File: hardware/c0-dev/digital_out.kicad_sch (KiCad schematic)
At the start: 27 parts, among them Q10 BSS138P, Q3 BSS138P, Q4 BSS138P, Q5 BSS138P, Q6 BSS138P, Q7 BSS138P, Q8 BSS138P, Q9 BSS138P, U34 B0505S-1WR3, U35 ISO1540, U36 TCA9555PWR, U48 TLP175A

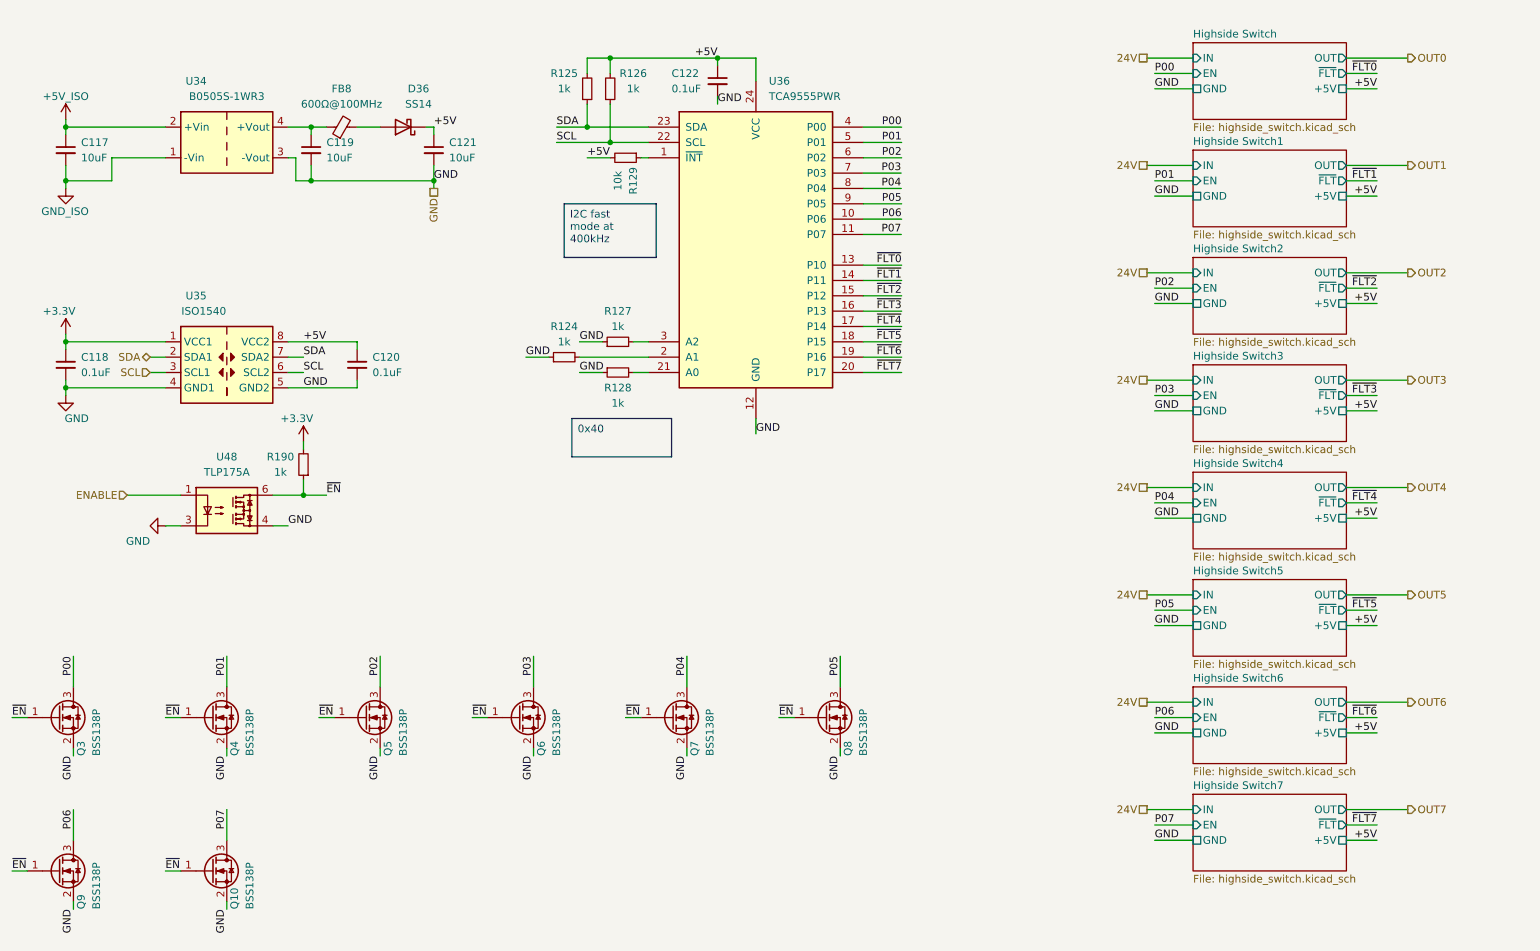
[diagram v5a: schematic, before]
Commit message: added 4-pin connector
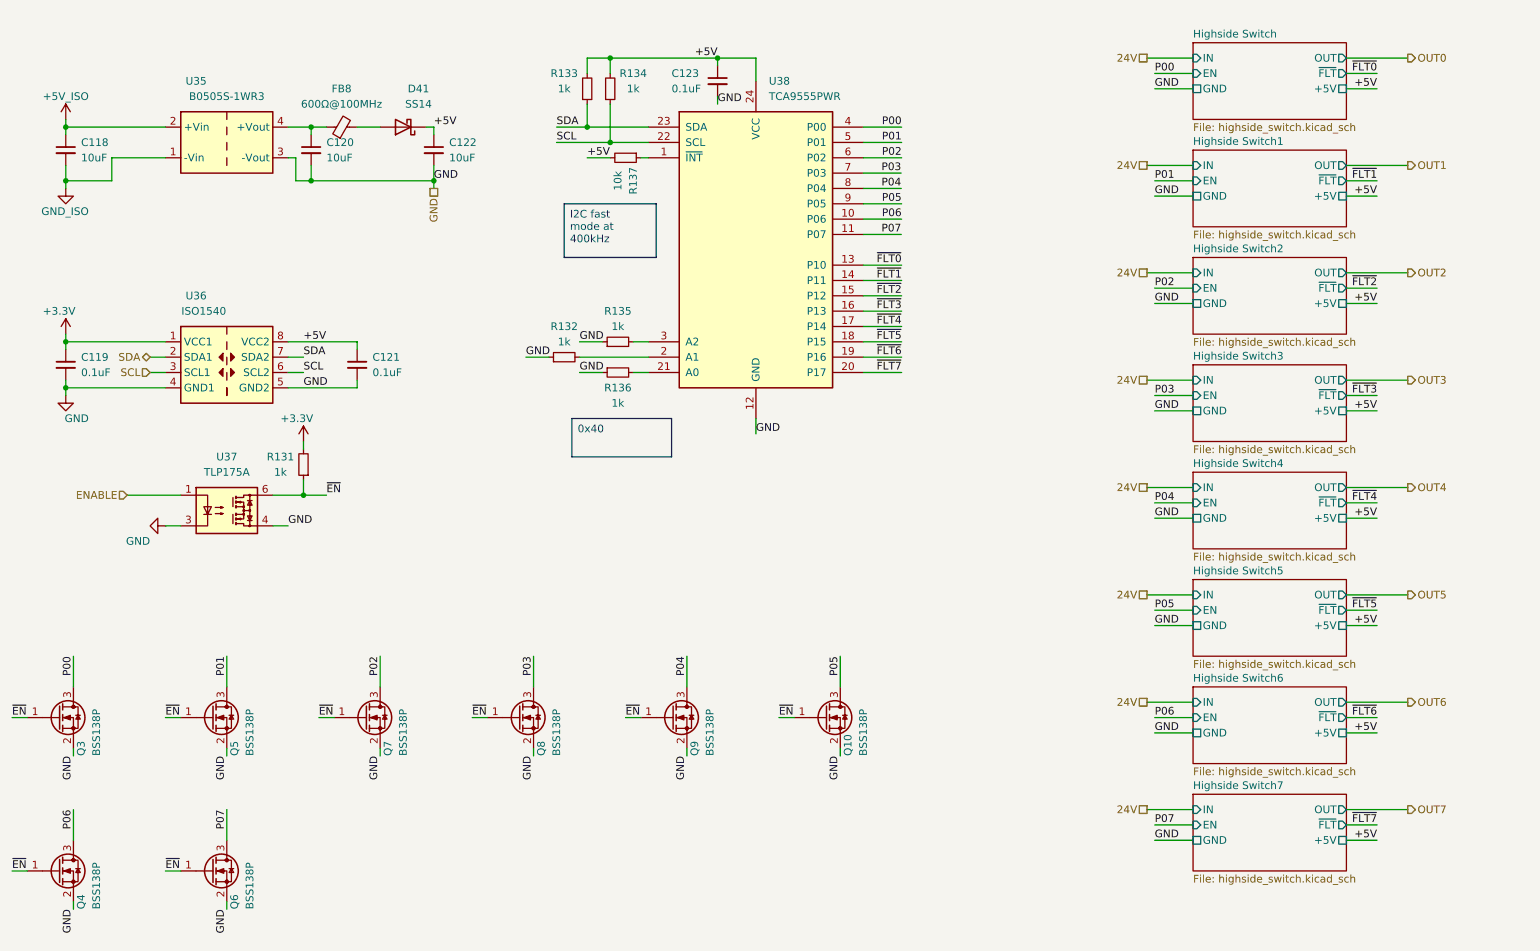
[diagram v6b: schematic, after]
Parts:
- renumbered C117 to C118, C118 to C119, C119 to C120, C120 to C121, C121 to C122, C122 to C123, D36 to D41, Q8 to Q10, Q9 to Q4, Q4 to Q5, Q10 to Q6, Q5 to Q7, Q6 to Q8, Q7 to Q9, R190 to R131, R124 to R132, R125 to R133, R126 to R134, R127 to R135, R128 to R136, R129 to R137, U34 to U35, U35 to U36, U48 to U37, U36 to U38

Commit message: annotation + new digital out
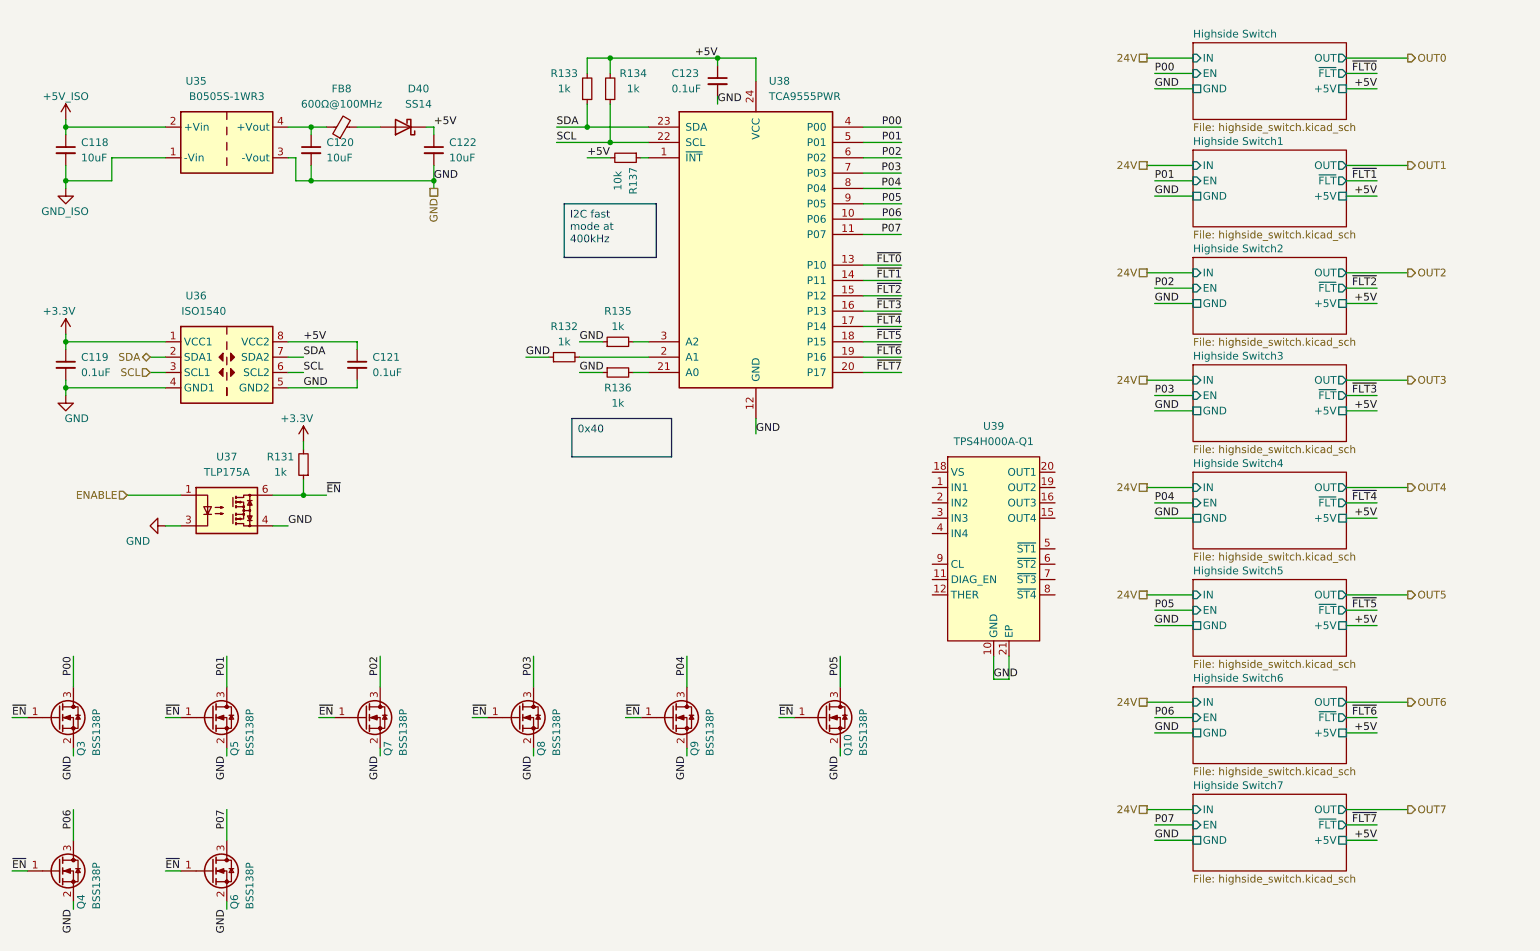
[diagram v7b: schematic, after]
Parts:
- added U39: TPS4H000A-Q1, Package_SO:ETSSOP-20-1EP_4.4x6.5mm_P0.65mm_EP3x4.2mm, symbol conduit:TPS4H000A-Q1
- renumbered D41 to D40
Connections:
- net GND: now also U39.10 (GND), U39.21 (EP)
- new net: U39.13 (NC), U39.14 (NC)
- new net VS: U39.17 (VS), U39.18 (VS)
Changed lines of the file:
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@@
 	(wire
 		(pts
+			(xy 193.04 127) (xy 193.04 123.19)
+		)
+		(stroke
+			(width 0)
+			(type default)
+		)
+	)
+	(wire
+		(pts
+			(xy 190.5 123.19) (xy 190.5 127)
+		)
+		(stroke
+			(width 0)
+			(type default)
+		)
+	)
+	(wire
+		(pts
 			(xy 97.79 44.45) (xy 97.79 45.72)
 		)
@@
 	(wire
 		(pts
+			(xy 190.5 127) (xy 193.04 127)
+		)
+		(stroke
+			(width 0)
+			(type default)
+		)
+	)
+	(wire
+		(pts
 			(xy 248.92 95.25) (xy 259.08 95.25)
 		)
@@
 		)
 	)
+	(label "GND"
+		(at 190.5 127 0)
+		(effects
+			(font
+				(size 1.27 1.27)
+			)
+			(justify left bottom)
+		)
+	)
 	(label "+5V"
 		(at 97.79 35.56 0)
@@
 	)
 	(symbol
+		(lib_id "conduit:TPS4H000A-Q1")
+		(at 190.5 104.14 0)
+		(unit 1)
+		(body_style 1)
+		(exclude_from_sim no)
+		(in_bom yes)
+		(on_board yes)
+		(in_pos_files yes)
+		(dnp no)
+		(fields_autoplaced yes)
+		(property "Reference" "U39"
+			(at 190.5 85.09 0)
+			(show_name no)
+			(do_not_autoplace no)
+			(effects
+				(font
+					(size 1.27 1.27)
+				)
+			)
+		)
+		(property "Value" "TPS4H000A-Q1"
+			(at 190.5 87.63 0)
+			(show_name no)
+			(do_not_autoplace no)
+			(effects
+				(font
+					(size 1.27 1.27)
+				)
+			)
+		)
+		(property "Footprint" "Package_SO:ETSSOP-20-1EP_4.4x6.5mm_P0.65mm_EP3x4.2mm"
+			(at 190.754 79.756 0)
+			(hide yes)
+			(show_name no)
+			(do_not_autoplace no)
+			(effects
+				(font
+					(size 1.27 1.27)
+				)
+			)
+		)
+		(property "Datasheet" "https://www.ti.com/lit/ds/symlink/tps4h000-q1.pdf"
+			(at 189.23 77.216 0)
+			(hide yes)
+			(show_name no)
+			(do_not_autoplace no)
+			(effects
+				(font
+					(size 1.27 1.27)
+				)
+			)
+		)
+		(property "Description" "40-V, 1-Ω, 4-ch automotive smart high-side switch with adjustable current limit"
+			(at 190.246 82.296 0)
+			(hide yes)
+			(show_name no)
+			(do_not_autoplace no)
+			(effects
+				(font
+					(size 1.27 1.27)
+				)
+			)
+		)
+		(property "JLCPCB Part" "C2680315"
+			(at 189.23 77.47 0)
+			(hide yes)
+			(show_name no)
+			(do_not_autoplace no)
+			(effects
+				(font
+					(size 1.27 1.27)
+				)
+			)
+		)
+		(pin "14"
+		)
+		(pin "13"
+		)
+		(pin "6"
+		)
+		(pin "12"
+		)
+		(pin "4"
+		)
+		(pin "3"
+		)
+		(pin "9"
+		)
+		(pin "10"
+		)
+		(pin "1"
+		)
+		(pin "2"
+		)
+		(pin "7"
+		)
+		(pin "8"
+		)
+		(pin "11"
+		)
+		(pin "5"
+		)
+		(pin "15"
+		)
+		(pin "16"
+		)
+		(pin "17"
+		)
+		(pin "18"
+		)
+		(pin "19"
+		)
+		(pin "20"
+		)
+		(pin "21"
+		)
+		(instances
+			(project "c0-dev"
+				(path "/b8347a0e-ad04-4414-969d-3c64a611d74e/680032e3-5da4-48ad-9c49-e468cbbeffb9"
+					(reference "U39")
+					(unit 1)
+				)
+			)
+		)
+	)
+	(symbol
 		(lib_id "Device:C_Small")
 		(at 144.78 27.94 0)
@@
 		(in_pos_files yes)
 		(dnp no)
-		(property "Reference" "D41"
+		(property "Reference" "D40"
 			(at 95.25 29.21 0)
 			(show_name no)
@@
 			(project "c0-dev"
 				(path "/b8347a0e-ad04-4414-969d-3c64a611d74e/680032e3-5da4-48ad-9c49-e468cbbeffb9"
-					(reference "D41")
+					(reference "D40")
 					(unit 1)
 				)

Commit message: updated digital out
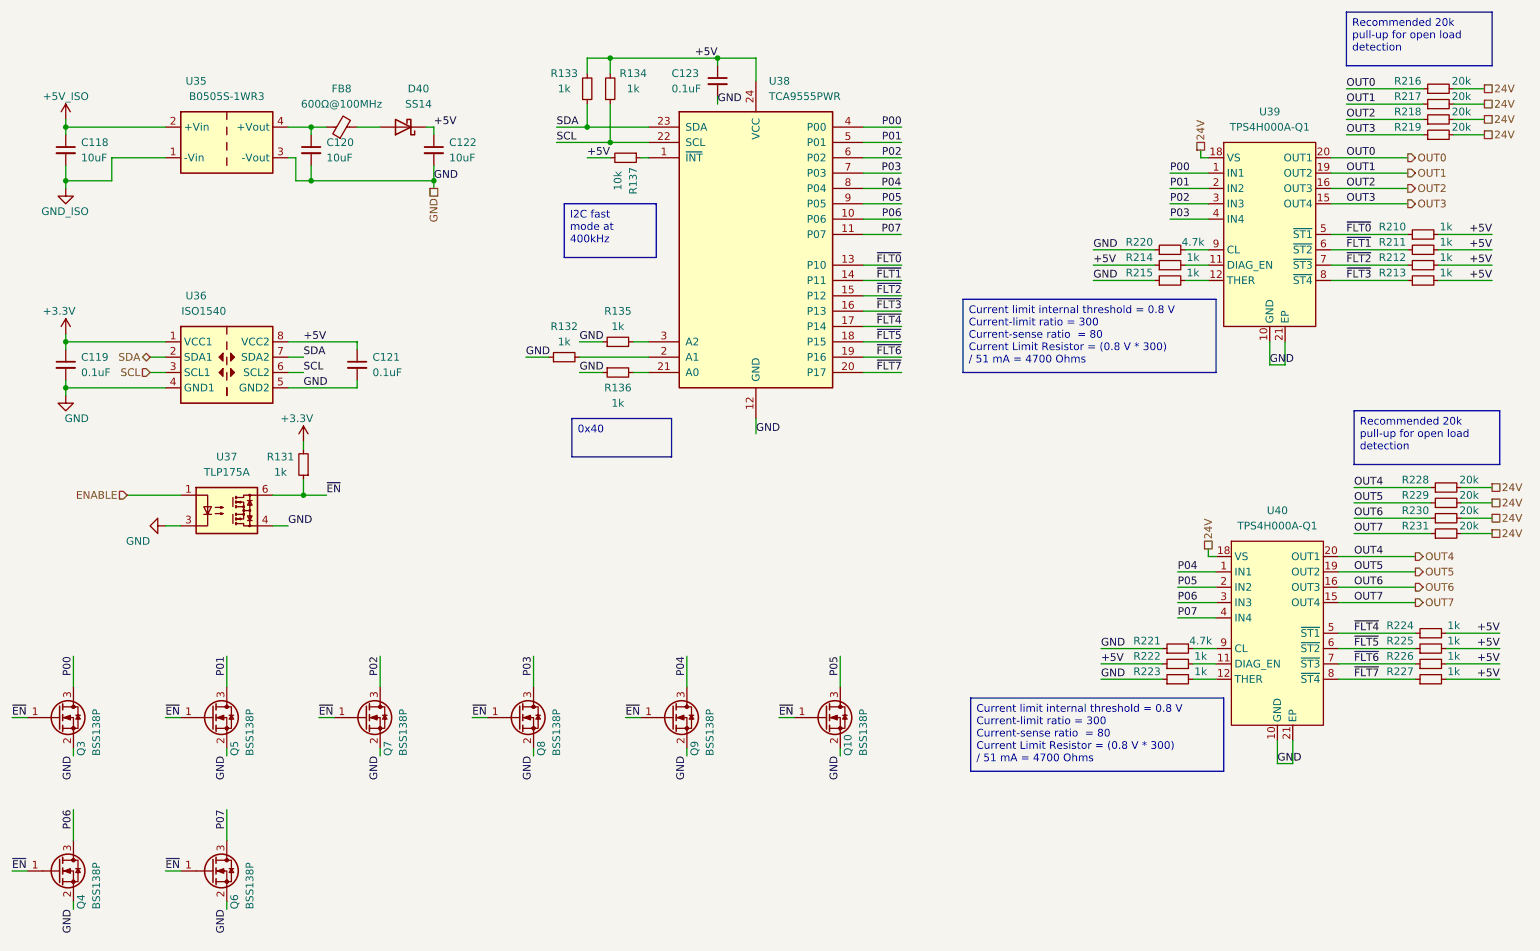
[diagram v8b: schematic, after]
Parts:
- added R210, R211, R212, R213, R214, R215, R222, R223, R224, R225, R226, R227: 1k, Resistor_SMD:R_0402_1005Metric, symbol Device:R_Small
- added R216, R217, R218, R219, R228, R229, R230, R231: 20k, Resistor_SMD:R_0402_1005Metric, symbol Device:R_Small
- added R220, R221: 4.7k, Resistor_SMD:R_0402_1005Metric, symbol Device:R_Small
- added U40: TPS4H000A-Q1, Package_SO:ETSSOP-20-1EP_4.4x6.5mm_P0.65mm_EP3x4.2mm, symbol conduit:TPS4H000A-Q1
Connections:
- net +5V: now also R210.2, R211.2, R212.2, R213.2, R214.1, R222.1, R224.2, R225.2, R226.2, R227.2
- net GND: now also R215.1, R220.1, R221.1, R223.1, U40.10 (GND), U40.21 (EP)
- net OUT0: now also U39.20 (OUT1), R216.1
- net OUT1: now also U39.19 (OUT2), R217.1
- net OUT2: now also U39.16 (OUT3), R218.1
- net OUT3: now also U39.15 (OUT4), R219.1
- net OUT4: now also R228.1, U40.20 (OUT1)
- net OUT5: now also R229.1, U40.19 (OUT2)
- net OUT6: now also R230.1, U40.16 (OUT3)
- net OUT7: now also R231.1, U40.15 (OUT4)
- net P00: now also U39.1 (IN1)
- net P01: now also U39.2 (IN2)
- net P02: now also U39.3 (IN3)
- net P03: now also U39.4 (IN4)
- net P04: now also U40.1 (IN1)
- net P05: now also U40.2 (IN2)
- net P06: now also U40.3 (IN3)
- net P07: now also U40.4 (IN4)
- net VS: now also R216.2, R217.2, R218.2, R219.2, R228.2, R229.2, R230.2, R231.2, U40.17 (VS), U40.18 (VS)
- net ~{FLT0}: now also U39.5 (~{ST1}), R210.1
- net ~{FLT1}: now also U39.6 (~{ST2}), R211.1
- net ~{FLT2}: now also U39.7 (~{ST3}), R212.1
- net ~{FLT3}: now also U39.8 (~{ST4}), R213.1
- net ~{FLT4}: now also R224.1, U40.5 (~{ST1})
- net ~{FLT5}: now also R225.1, U40.6 (~{ST2})
- net ~{FLT6}: now also R226.1, U40.7 (~{ST3})
- net ~{FLT7}: now also R227.1, U40.8 (~{ST4})
- net at U39.11 (DIAG_EN): now also R214.2
- net at U39.12 (THER): now also R215.2
- net at U39.9 (CL): now also R220.2
- new net: R222.2, U40.11 (DIAG_EN)
- new net: R223.2, U40.12 (THER)
- new net: U40.13 (NC), U40.14 (NC)
- new net: R221.2, U40.9 (CL)
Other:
- removed sheet Highside Switch
- removed sheet Highside Switch1
- removed sheet Highside Switch2
- removed sheet Highside Switch3
- removed sheet Highside Switch4
- removed sheet Highside Switch5
- removed sheet Highside Switch6
- removed sheet Highside Switch7
- moved on the sheet: U39
